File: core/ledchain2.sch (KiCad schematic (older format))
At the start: 20 parts, among them U63 WS2811, U64 WS2811, U65 WS2811, U66 WS2811, U67 WS2811, U68 WS2811, U69 WS2811, U70 WS2811, U71 WS2811, U72 WS2811

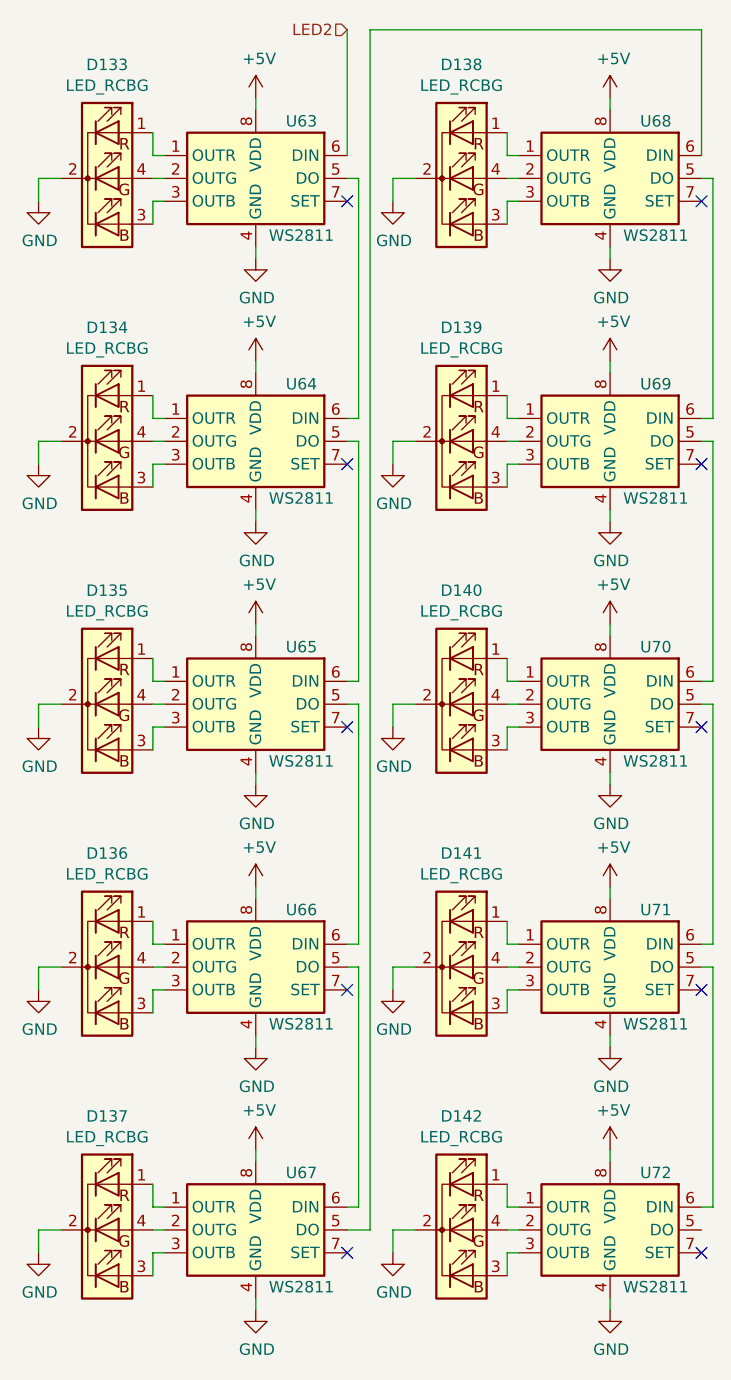
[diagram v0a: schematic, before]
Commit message: Fixed ERC errors and initially populated board
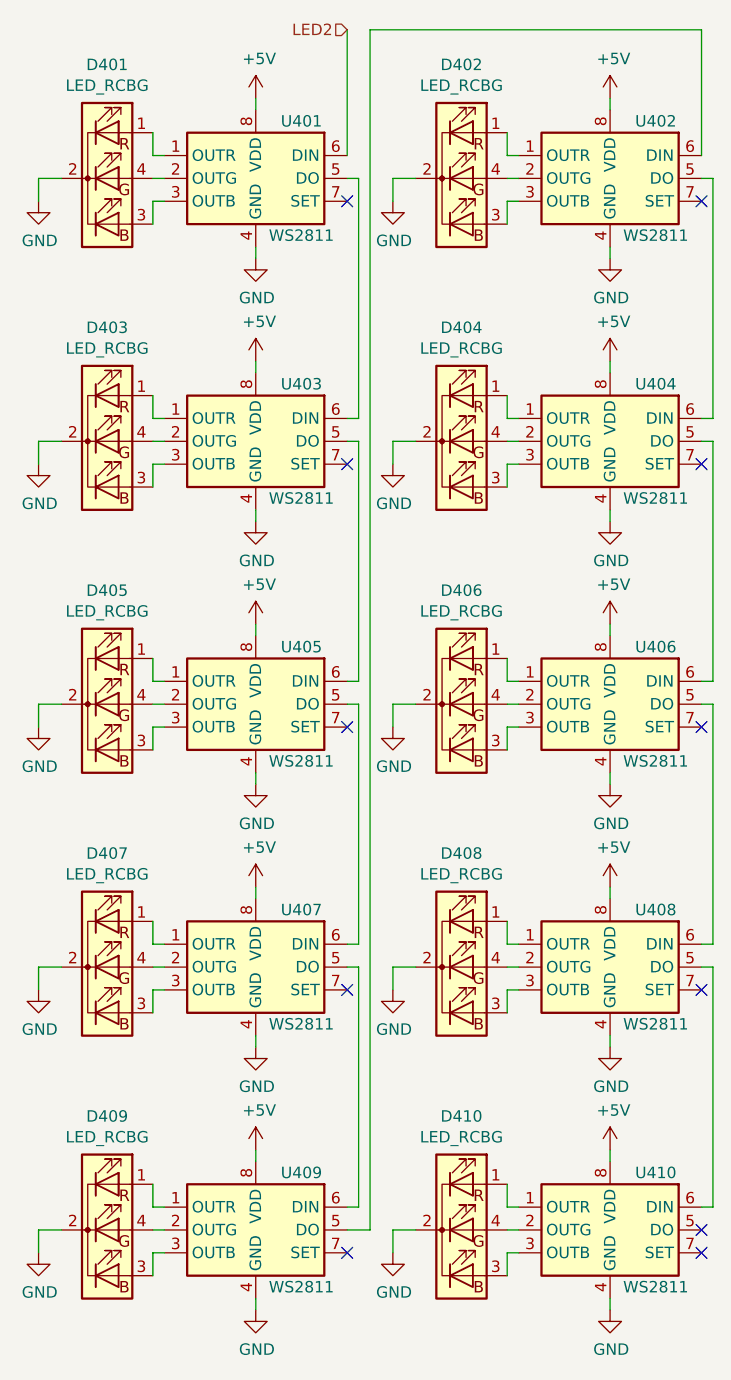
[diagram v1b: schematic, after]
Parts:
- renumbered D133 to D401, D138 to D402, D134 to D403, D139 to D404, D135 to D405, D140 to D406, D136 to D407, D141 to D408, D137 to D409, D142 to D410, U63 to U401, U68 to U402, U64 to U403, U69 to U404, U65 to U405, U70 to U406, U66 to U407, U71 to U408, U67 to U409, U72 to U410
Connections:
- no-connect marks 10 -> 11
